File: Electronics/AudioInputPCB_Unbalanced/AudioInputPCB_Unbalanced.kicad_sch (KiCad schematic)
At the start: 117 parts, among them J1 IDC, J2 RCA x2, J3 RCA x2, J4 RCA x2, J5 RCA x2, U1 NE5532, U2 NE5532, U3 NE5532, U4 NE5532

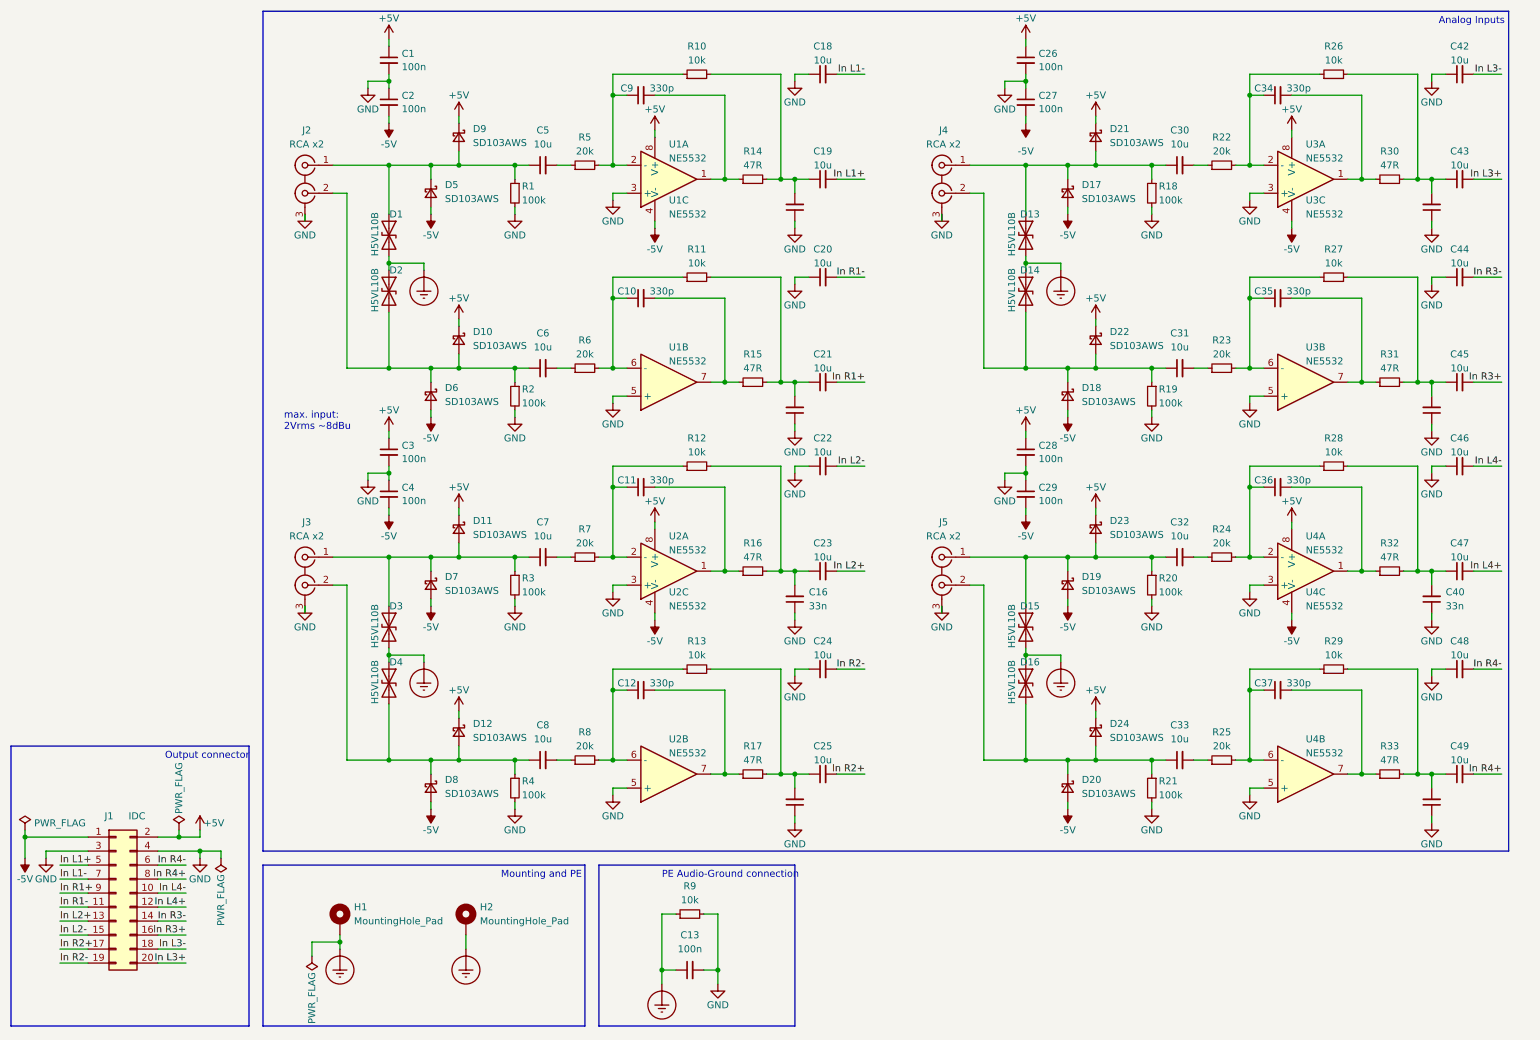
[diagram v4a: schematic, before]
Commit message: Adds AES17 measurements for rev1 of maxi. adds first iteration of maxi firmware. prototype now functional. adds mechanical information such as pcb 3d models and datasheets for psu and power switch, -connector.
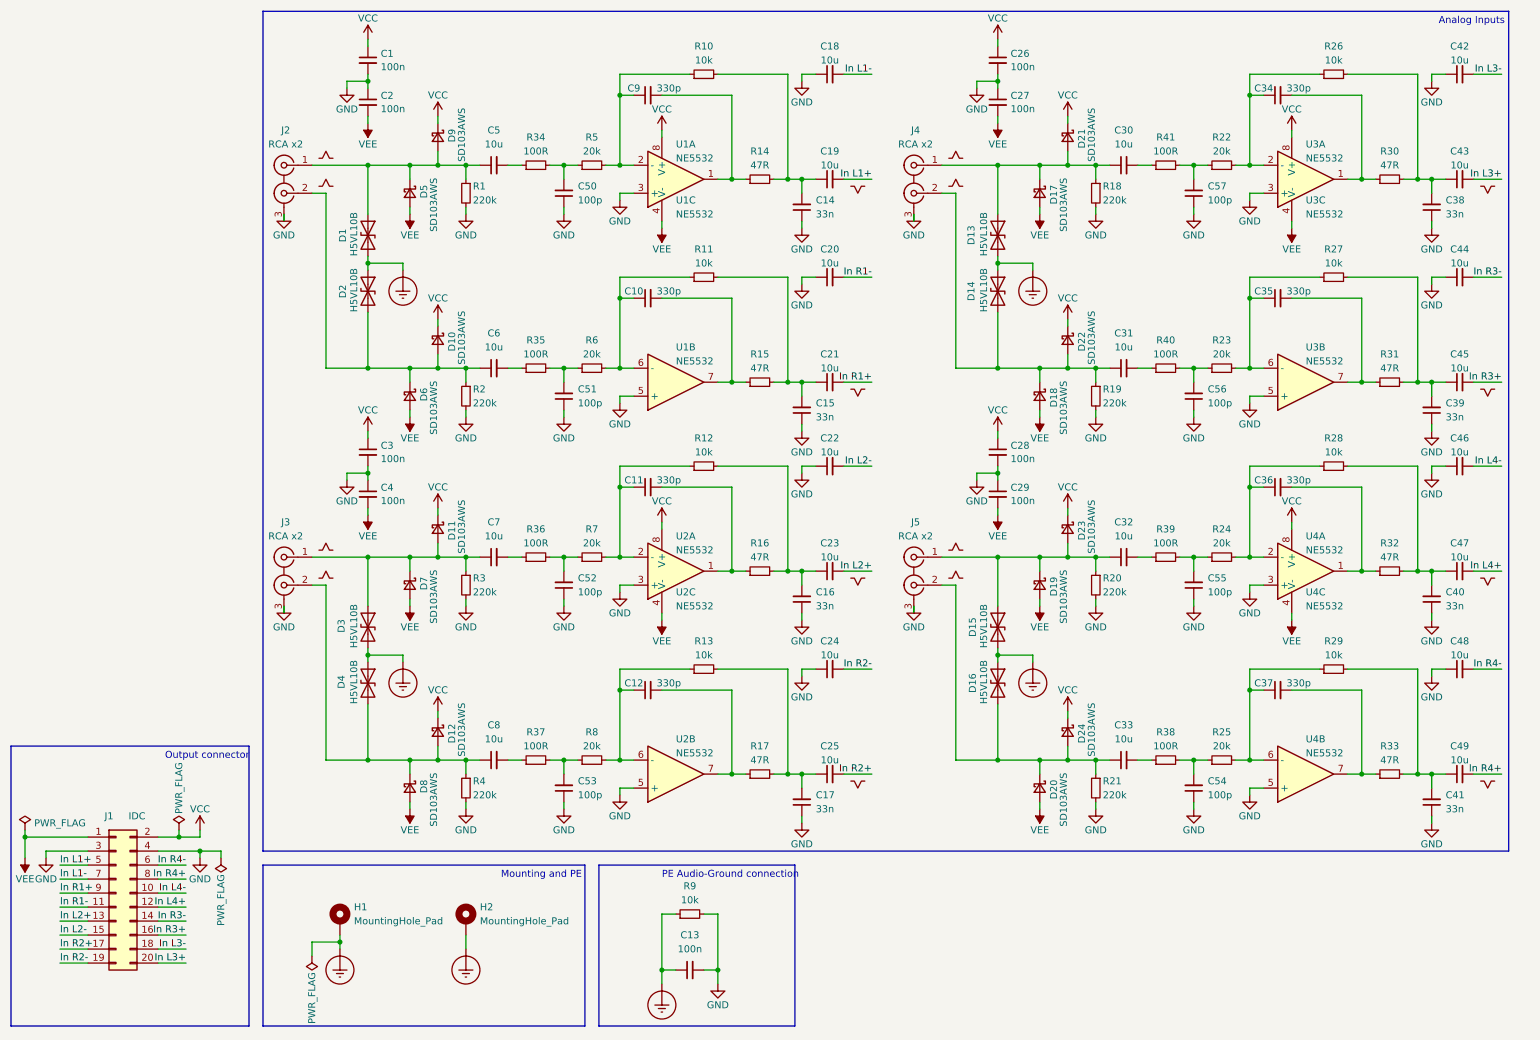
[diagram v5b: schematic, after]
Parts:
- added C50, C51, C52, C53, C54, C55, C56, C57: 100p, Capacitor_SMD:C_0402_1005Metric, symbol Device:C_Small
- added Label1, Label10, Label11, Label12, Label13, Label14, Label15, Label16, Label2, Label3, Label4, Label5, Label6, Label7, Label8, Label9: ~, symbol 1_ProjectSymbols:phase
- added R34, R35, R36, R37, R38, R39, R40, R41: 100R, Resistor_SMD:R_0402_1005Metric, symbol Device:R_Small
- R1, R18, R19, R2, R20, R21, R3, R4: value 100k -> 220k; LCSC Part # C25741 -> C25767; Part Number 0402WGF1003TCE -> 0402WGF2203TCE
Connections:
- net GND: now also C50.1, C51.1, C52.1, C53.1, C54.1, C55.1, C56.1, C57.1
- net at C32.2: now also R39.1; no longer R24.1
- net at R6.1: now also C51.2, R35.2; no longer C6.2
- net at C7.2: now also R36.1; no longer R7.1
- net at R5.1: now also C50.2, R34.2; no longer C5.2
- net at R22.1: now also C57.2, R41.2; no longer C30.2
- net at C31.2: now also R40.1; no longer R23.1
- net at R8.1: now also C53.2, R37.2; no longer C8.2
- net at R25.1: now also C54.2, R38.2; no longer C33.2
- net +5V renamed VCC
- net -5V renamed VEE
- new net: C56.2, R23.1, R40.2
- new net: C30.2, R41.1
- new net: C33.2, R38.1
- new net: C55.2, R24.1, R39.2
- new net: C5.2, R34.1
- new net: C8.2, R37.1
- new net: C6.2, R35.1
- new net: C52.2, R36.2, R7.1
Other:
- note removed: "max. input: 2Vrms ~8dBu"
- moved on the sheet: C1, C10, C11, C12, C16, C18, C19, C2, C20, C21, C22, C23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
